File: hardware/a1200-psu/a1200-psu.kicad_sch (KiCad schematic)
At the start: 61 parts, among them J1 220V, J2 Conn_01x05, Q1 P2N60, SW1 SW_SPST, U1 UC3844_DIP8, U2 PC817, U3 TL431D

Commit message: Add more components to PCB
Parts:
- C2, C3, C7, C8: footprint (none) -> Capacitor_THT:C_Rect_L11.0mm_W2.8mm_P10.00mm_MKT
- C5, C6: value 220n -> 220nF; footprint (none) -> Capacitor_THT:C_Rect_L28.0mm_W8.0mm_P22.50mm_MKS4
- D4: footprint (none) -> Amiga 1200:Diode_Bridge
- F1: footprint (none) -> Fuse:Fuseholder_Cylinder-5x20mm_Schurter_0031_8201_Horizontal_Open
- J1: symbol Amiga A1200:AC_IN -> Amiga 1200:AC-In
- SW1: now left out of the parts list
- TH1: footprint (none) -> Resistor_THT:R_Axial_DIN0207_L6.3mm_D2.5mm_P7.62mm_Horizontal
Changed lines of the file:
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@@
     (property "Reference" "F1" (id 0) (at 121.92 82.55 90))
     (property "Value" "250V T 1A" (id 1) (at 121.92 85.09 90))
-    (property "Footprint" "" (id 2) (at 121.92 90.678 90)
+    (property "Footprint" "Fuse:Fuseholder_Cylinder-5x20mm_Schurter_0031_8201_Horizontal_Open" (id 2) (at 121.92 90.678 90)
       (effects (font (size 1.27 1.27)) hide)
     )
@@
       (effects (font (size 1.27 1.27)) (justify left))
     )
-    (property "Value" "220n" (id 1) (at 146.05 91.4462 0)
-      (effects (font (size 1.27 1.27)) (justify left))
-    )
-    (property "Footprint" "" (id 2) (at 143.51 90.17 0)
+    (property "Value" "220nF" (id 1) (at 146.05 91.4462 0)
+      (effects (font (size 1.27 1.27)) (justify left))
+    )
+    (property "Footprint" "Capacitor_THT:C_Rect_L28.0mm_W8.0mm_P22.50mm_MKS4" (id 2) (at 143.51 90.17 0)
       (effects (font (size 1.27 1.27)) hide)
     )
@@
   )
   (symbol (lib_id "Switch:SW_SPST") (at 109.22 88.9 0) (unit 1)
-    (in_bom yes) (on_board yes) (fields_autoplaced)
+    (in_bom no) (on_board yes) (fields_autoplaced)
     (property "Reference" "SW1" (id 0) (at 109.22 82.55 0))
     (property "Value" "SW_SPST" (id 1) (at 109.22 85.09 0))
@@
       (effects (font (size 1.27 1.27)) (justify right))
     )
-    (property "Footprint" "" (id 2) (at 127 99.06 0)
+    (property "Footprint" "Capacitor_THT:C_Rect_L11.0mm_W2.8mm_P10.00mm_MKT" (id 2) (at 127 99.06 0)
       (effects (font (size 1.27 1.27)) hide)
     )
@@
       (effects (font (size 1.27 1.27)) (justify left))
     )
-    (property "Footprint" "" (id 2) (at 177.8 86.36 0)
+    (property "Footprint" "Capacitor_THT:C_Rect_L11.0mm_W2.8mm_P10.00mm_MKT" (id 2) (at 177.8 86.36 0)
       (effects (font (size 1.27 1.27)) hide)
     )
@@
     (pin "1")
   )
-  (symbol (lib_id "Amiga A1200:AC_IN") (at 95.25 91.44 0) (mirror y) (unit 1)
+  (symbol (lib_id "Amiga 1200:AC-In") (at 95.25 91.44 0) (mirror y) (unit 1)
     (in_bom yes) (on_board yes) (fields_autoplaced)
     (property "Reference" "J1" (id 0) (at 95.25 82.55 0))
@@
       (effects (font (size 1.27 1.27)) (justify left))
     )
-    (property "Footprint" "" (id 2) (at 194.31 90.17 0)
+    (property "Footprint" "Amiga 1200:Diode_Bridge" (id 2) (at 194.31 90.17 0)
       (effects (font (size 1.27 1.27)) hide)
     )
@@
       (effects (font (size 1.27 1.27)) (justify left))
     )
-    (property "Footprint" "" (id 2) (at 177.8 101.6 0)
+    (property "Footprint" "Capacitor_THT:C_Rect_L11.0mm_W2.8mm_P10.00mm_MKT" (id 2) (at 177.8 101.6 0)
       (effects (font (size 1.27 1.27)) hide)
     )
@@
     (property "Reference" "TH1" (id 0) (at 133.6675 80.01 90))
     (property "Value" "30R" (id 1) (at 133.6675 82.55 90))
-    (property "Footprint" "" (id 2) (at 132.08 88.9 0)
+    (property "Footprint" "Resistor_THT:R_Axial_DIN0207_L6.3mm_D2.5mm_P7.62mm_Horizontal" (id 2) (at 132.08 88.9 0)
       (effects (font (size 1.27 1.27)) hide)
     )
@@
       (effects (font (size 1.27 1.27)) (justify right))
     )
-    (property "Value" "220n" (id 1) (at 168.91 91.4462 0)
-      (effects (font (size 1.27 1.27)) (justify right))
-    )
-    (property "Footprint" "" (id 2) (at 171.45 90.17 0)
+    (property "Value" "220nF" (id 1) (at 168.91 91.4462 0)
+      (effects (font (size 1.27 1.27)) (justify right))
+    )
+    (property "Footprint" "Capacitor_THT:C_Rect_L28.0mm_W8.0mm_P22.50mm_MKS4" (id 2) (at 171.45 90.17 0)
       (effects (font (size 1.27 1.27)) hide)
     )
@@
       (effects (font (size 1.27 1.27)) (justify left))
     )
-    (property "Footprint" "" (id 2) (at 118.11 99.06 0)
+    (property "Footprint" "Capacitor_THT:C_Rect_L11.0mm_W2.8mm_P10.00mm_MKT" (id 2) (at 118.11 99.06 0)
       (effects (font (size 1.27 1.27)) hide)
     )
@@
     )
     (path "/f95f2ed1-f741-46d5-97f4-bab25cb5cc46"
-      (reference "C2") (unit 1) (value "4n7") (footprint "")
+      (reference "C2") (unit 1) (value "4n7") (footprint "Capacitor_THT:C_Rect_L11.0mm_W2.8mm_P10.00mm_MKT")
     )
     (path "/9d654ae6-012f-4a48-9ba5-5698e397d928"
-      (reference "C3") (unit 1) (value "4n7") (footprint "")
+      (reference "C3") (unit 1) (value "4n7") (footprint "Capacitor_THT:C_Rect_L11.0mm_W2.8mm_P10.00mm_MKT")
     )
     (path "/27ab0d51-ef78-4fc4-9734-e35d1c063136"
@@
     )
     (path "/78df1e25-c3ee-40dc-a712-abf386a892cf"
-      (reference "C5") (unit 1) (value "220n") (footprint "")
+      (reference "C5") (unit 1) (value "220nF") (footprint "Capacitor_THT:C_Rect_L28.0mm_W8.0mm_P22.50mm_MKS4")
     )
     (path "/dc9cd73a-5767-45ed-b0d4-e0dea089895b"
-      (reference "C6") (unit 1) (value "220n") (footprint "")
+      (reference "C6") (unit 1) (value "220nF") (footprint "Capacitor_THT:C_Rect_L28.0mm_W8.0mm_P22.50mm_MKS4")
     )
     (path "/a4e49ea5-96a7-406c-91fc-4da04c66d09f"
-      (reference "C7") (unit 1) (value "4n7") (footprint "")
+      (reference "C7") (unit 1) (value "4n7") (footprint "Capacitor_THT:C_Rect_L11.0mm_W2.8mm_P10.00mm_MKT")
     )
     (path "/cf3de267-b17e-4a71-968f-bc3d21c0891d"
-      (reference "C8") (unit 1) (value "4n7") (footprint "")
+      (reference "C8") (unit 1) (value "4n7") (footprint "Capacitor_THT:C_Rect_L11.0mm_W2.8mm_P10.00mm_MKT")
     )
     (path "/ee9b13c8-7d9f-4c1f-8502-54c994d534b2"
@@
     )
     (path "/bfe1a8e1-50be-4800-9ea3-a889eb81384c"
-      (reference "D4") (unit 1) (value "1N4007") (footprint "")
+      (reference "D4") (unit 1) (value "1N4007") (footprint "Amiga 1200:Diode_Bridge")
     )
     (path "/e4cc2bf7-eab8-4273-a682-53361c658daa"
@@
     )
     (path "/2342b295-a7df-4f3f-9757-7c891741f4c4"
-      (reference "F1") (unit 1) (value "250V T 1A") (footprint "")
+      (reference "F1") (unit 1) (value "250V T 1A") (footprint "Fuse:Fuseholder_Cylinder-5x20mm_Schurter_0031_8201_Horizontal_Open")
     )
     (path "/bcd00d62-58ab-42ee-8226-ab8ed47671c3"
@@
     )
     (path "/d6fefacf-6940-45a2-b279-0f7149851875"
-      (reference "TH1") (unit 1) (value "30R") (footprint "")
+      (reference "TH1") (unit 1) (value "30R") (footprint "Resistor_THT:R_Axial_DIN0207_L6.3mm_D2.5mm_P7.62mm_Horizontal")
     )
     (path "/32bac948-60ce-4bc5-be71-ae7e97ee9e18"

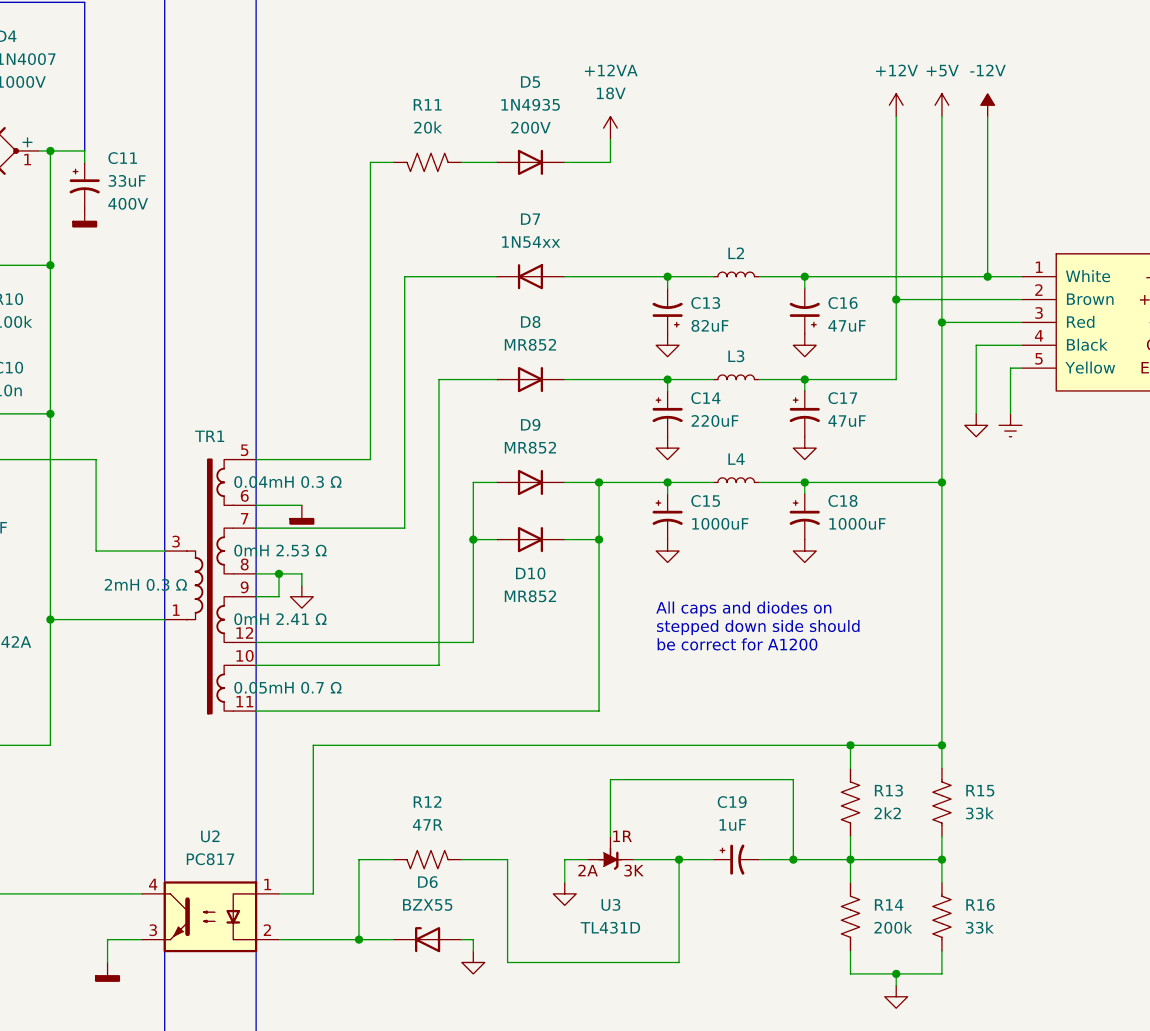
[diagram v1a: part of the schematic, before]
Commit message: Finished PCB and add missing parts
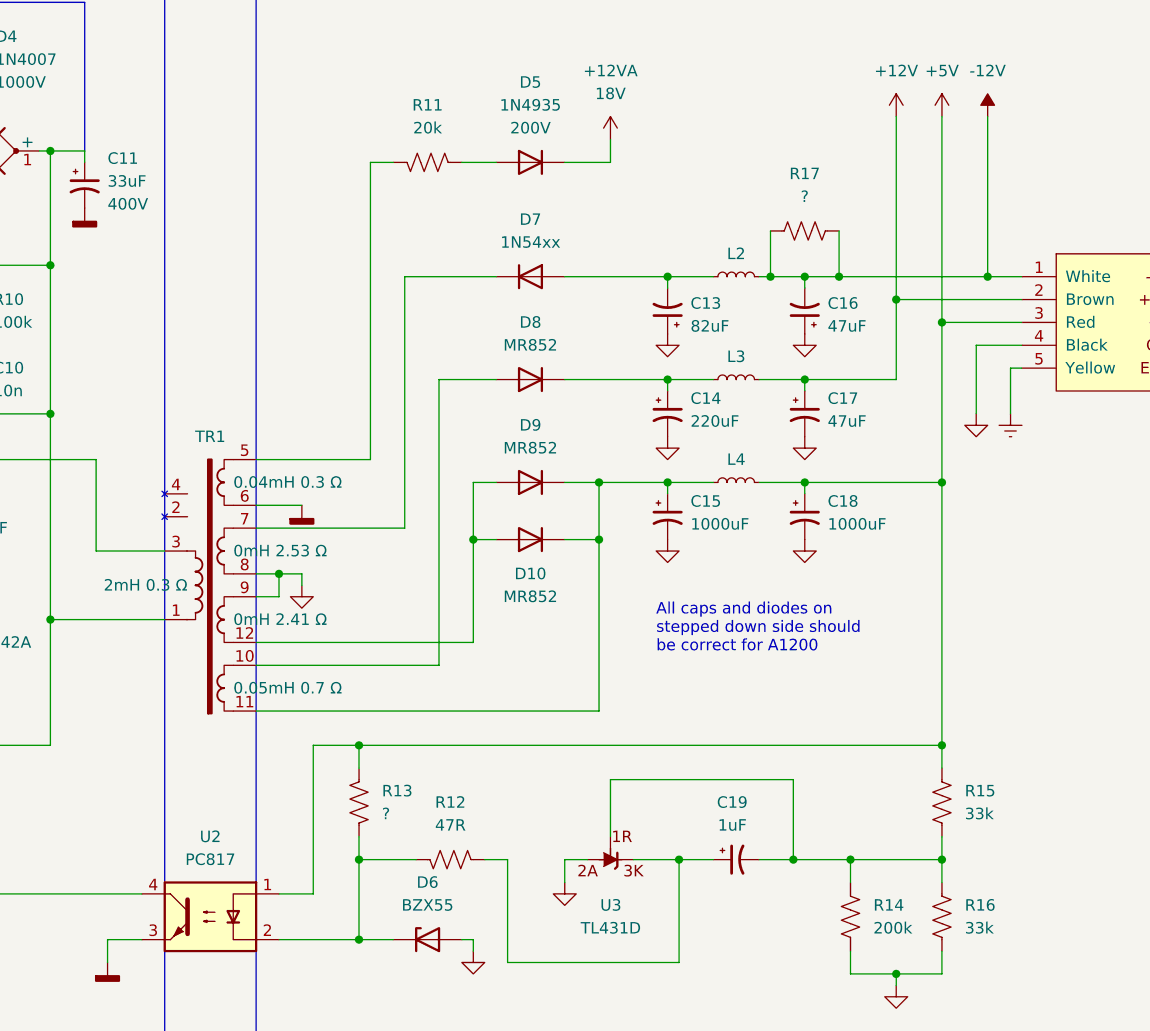
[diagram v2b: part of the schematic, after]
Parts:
- added R17: ?, Resistor_THT:R_Axial_DIN0309_L9.0mm_D3.2mm_P12.70mm_Horizontal, symbol Device:R_US
- C13, C16, C17, C19: footprint (none) -> Capacitor_THT:CP_Radial_D4.0mm_P1.50mm
- C14: footprint (none) -> Capacitor_THT:CP_Radial_D5.0mm_P2.50mm
- C15, C18: footprint (none) -> Capacitor_THT:CP_Radial_D8.0mm_P5.00mm
- D10, D7, D8, D9: footprint (none) -> Diode_THT:D_5W_P12.70mm_Horizontal
- D5: footprint (none) -> Diode_THT:D_DO-41_SOD81_P10.16mm_Horizontal
- D6: footprint (none) -> Diode_THT:D_DO-35_SOD27_P10.16mm_Horizontal
- J1: footprint (none) -> Connector_PinHeader_2.54mm:PinHeader_1x03_P2.54mm_Vertical; now left out of the parts list
- J2: footprint (none) -> Connector_PinHeader_2.54mm:PinHeader_1x05_P2.54mm_Vertical
- L2, L3, L4: footprint (none) -> Inductor_THT:L_Radial_D6.0mm_P4.00mm
- R12: footprint (none) -> Resistor_THT:R_Axial_DIN0309_L9.0mm_D3.2mm_P12.70mm_Horizontal
- R13: value 2k2 -> ?; footprint (none) -> Resistor_THT:R_Axial_DIN0207_L6.3mm_D2.5mm_P10.16mm_Horizontal
- R14, R15, R16: footprint (none) -> Resistor_THT:R_Axial_DIN0204_L3.6mm_D1.6mm_P5.08mm_Horizontal
- U3: footprint Package_TO_SOT_THT:TO-92L -> Package_TO_SOT_THT:TO-92
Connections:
- net -12V: now also R17.1, R17.2
- net GND: no longer U3.3 (A), U3.6 (A), U3.7 (A)
- net at C19.2, R14.2, R15.1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: now also U3.1 (REF); no longer R13.1, U3.8 (REF)
- net at D6.1 (K), R12.1, U2.2: now also R13.1
- net at C19.1, R12.2: now also U3.3 (K); no longer U3.1 (K)
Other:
- moved on the sheet: R12

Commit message: Replace pin headers with terminals
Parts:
- J1: footprint Connector_PinHeader_2.54mm:PinHeader_1x03_P2.54mm_Vertical -> TerminalBlock_Phoenix:TerminalBlock_Phoenix_MPT-0,5-3-2.54_1x03_P2.54mm_Horizontal
- J2: footprint Connector_PinHeader_2.54mm:PinHeader_1x05_P2.54mm_Vertical -> TerminalBlock_Phoenix:TerminalBlock_Phoenix_MPT-0,5-5-2.54_1x05_P2.54mm_Horizontal
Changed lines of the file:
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@@
       (effects (font (size 1.27 1.27)) (justify left) hide)
     )
-    (property "Footprint" "Connector_PinHeader_2.54mm:PinHeader_1x05_P2.54mm_Vertical" (id 2) (at 316.23 109.22 0)
+    (property "Footprint" "TerminalBlock_Phoenix:TerminalBlock_Phoenix_MPT-0,5-5-2.54_1x05_P2.54mm_Horizontal" (id 2) (at 316.23 109.22 0)
       (effects (font (size 1.27 1.27)) hide)
     )
@@
     (property "Reference" "J1" (id 0) (at 95.25 82.55 0))
     (property "Value" "220V" (id 1) (at 95.25 85.09 0))
-    (property "Footprint" "Connector_PinHeader_2.54mm:PinHeader_1x03_P2.54mm_Vertical" (id 2) (at 95.25 91.44 0)
+    (property "Footprint" "TerminalBlock_Phoenix:TerminalBlock_Phoenix_MPT-0,5-3-2.54_1x03_P2.54mm_Horizontal" (id 2) (at 95.25 91.44 0)
       (effects (font (size 1.27 1.27)) hide)
     )
@@
     )
     (path "/bcd00d62-58ab-42ee-8226-ab8ed47671c3"
-      (reference "J1") (unit 1) (value "220V") (footprint "Connector_PinHeader_2.54mm:PinHeader_1x03_P2.54mm_Vertical")
+      (reference "J1") (unit 1) (value "220V") (footprint "TerminalBlock_Phoenix:TerminalBlock_Phoenix_MPT-0,5-3-2.54_1x03_P2.54mm_Horizontal")
     )
     (path "/00000000-0000-0000-0000-00005e7024e2"
-      (reference "J2") (unit 1) (value "Conn_01x05") (footprint "Connector_PinHeader_2.54mm:PinHeader_1x05_P2.54mm_Vertical")
+      (reference "J2") (unit 1) (value "Conn_01x05") (footprint "TerminalBlock_Phoenix:TerminalBlock_Phoenix_MPT-0,5-5-2.54_1x05_P2.54mm_Horizontal")
     )
     (path "/843a1a7e-3157-4032-a526-52baa7686c09"

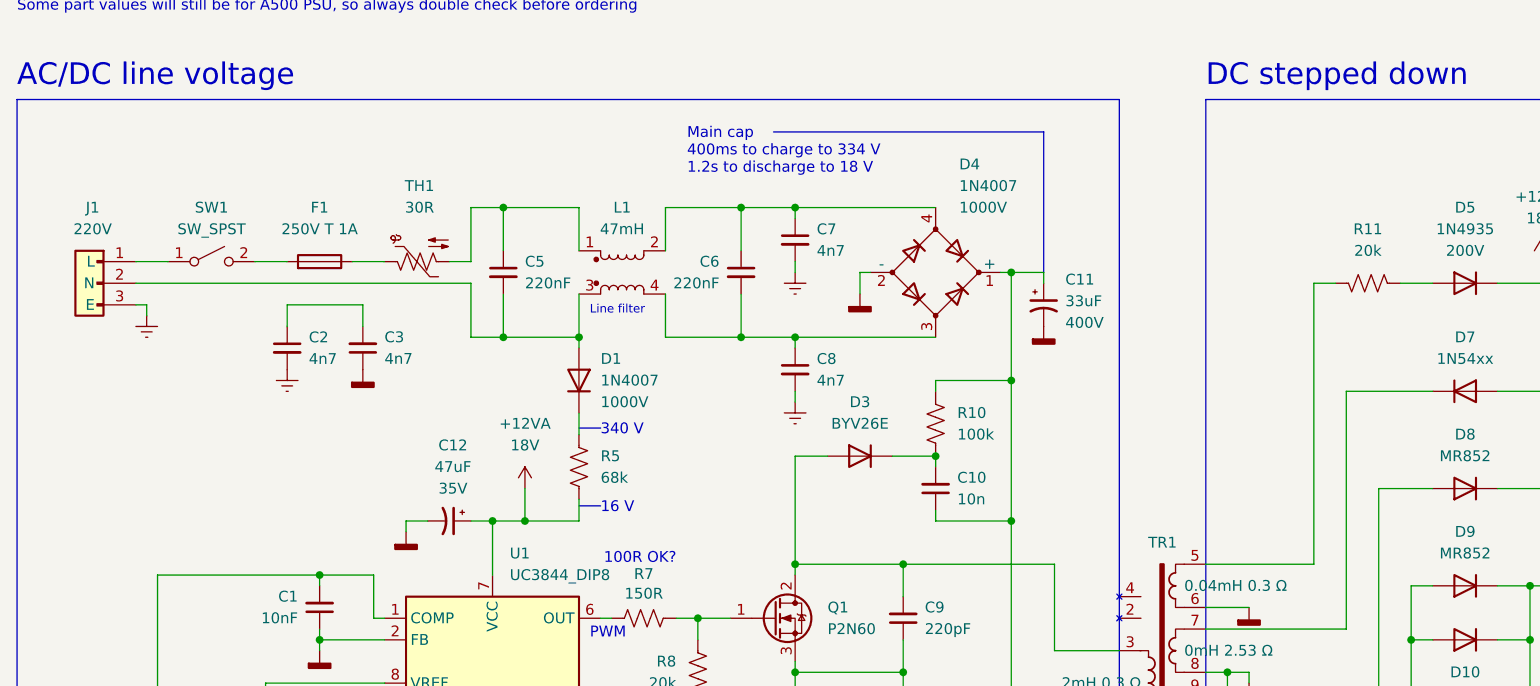
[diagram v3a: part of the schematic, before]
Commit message: Fixed various PCB layout errors
Also fixed:
- R value
- Live/PWM IC connection
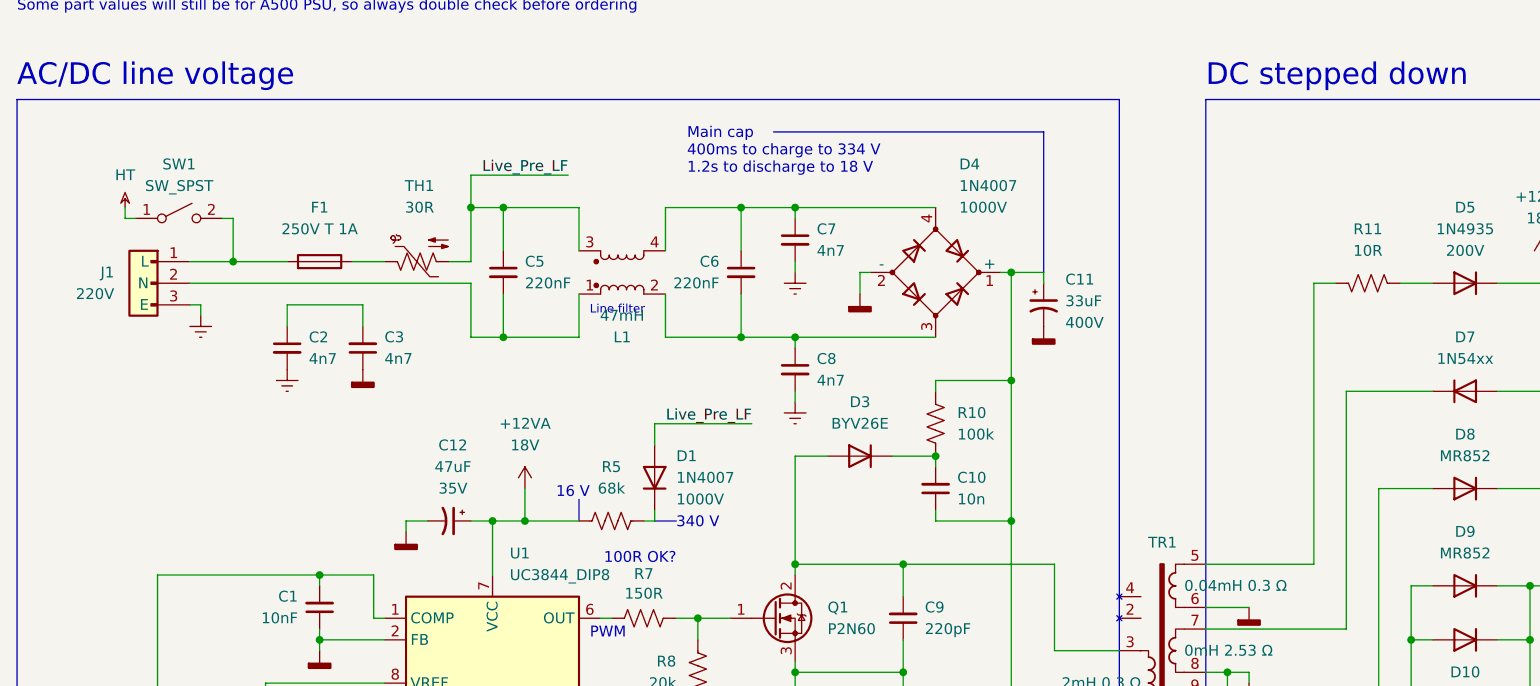
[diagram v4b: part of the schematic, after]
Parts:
- J1: footprint TerminalBlock_Phoenix:TerminalBlock_Phoenix_MPT-0,5-3-2.54_1x03_P2.54mm_Horizontal -> TerminalBlock_Phoenix:TerminalBlock_Phoenix_PT-1,5-3-3.5-H_1x03_P3.50mm_Horizontal
- R11: value 20k -> 10R
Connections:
- net +12VA: now also R5.1; no longer R5.2
- net at F1.2, SW1.2 (B): now also J1.1 (L)
- net Live_Pre_LF: now reaches C5.1, TH1.2
- net Live_Pre_LF: now also D1.2 (A), L1.3; no longer L1.1
- net at C5.2, J1.2 (N): now also L1.1; no longer D1.2 (A), L1.3
- net at C6.1, C7.1, D4.4: now also L1.4; no longer L1.2
- net at C6.2, C8.1, D4.3: now also L1.2; no longer L1.4
- net HT: now reaches SW1.1 (A)
- net HT: no longer J1.1 (L)
- net at D1.1 (K): now also R5.2; no longer R5.1
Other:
- moved on the sheet: D1, J1
